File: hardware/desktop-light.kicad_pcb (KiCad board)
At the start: 2 copper layers, 100 x 100 mm, 56 parts, among them J1 Conn_01x06, J2 Conn_01x06

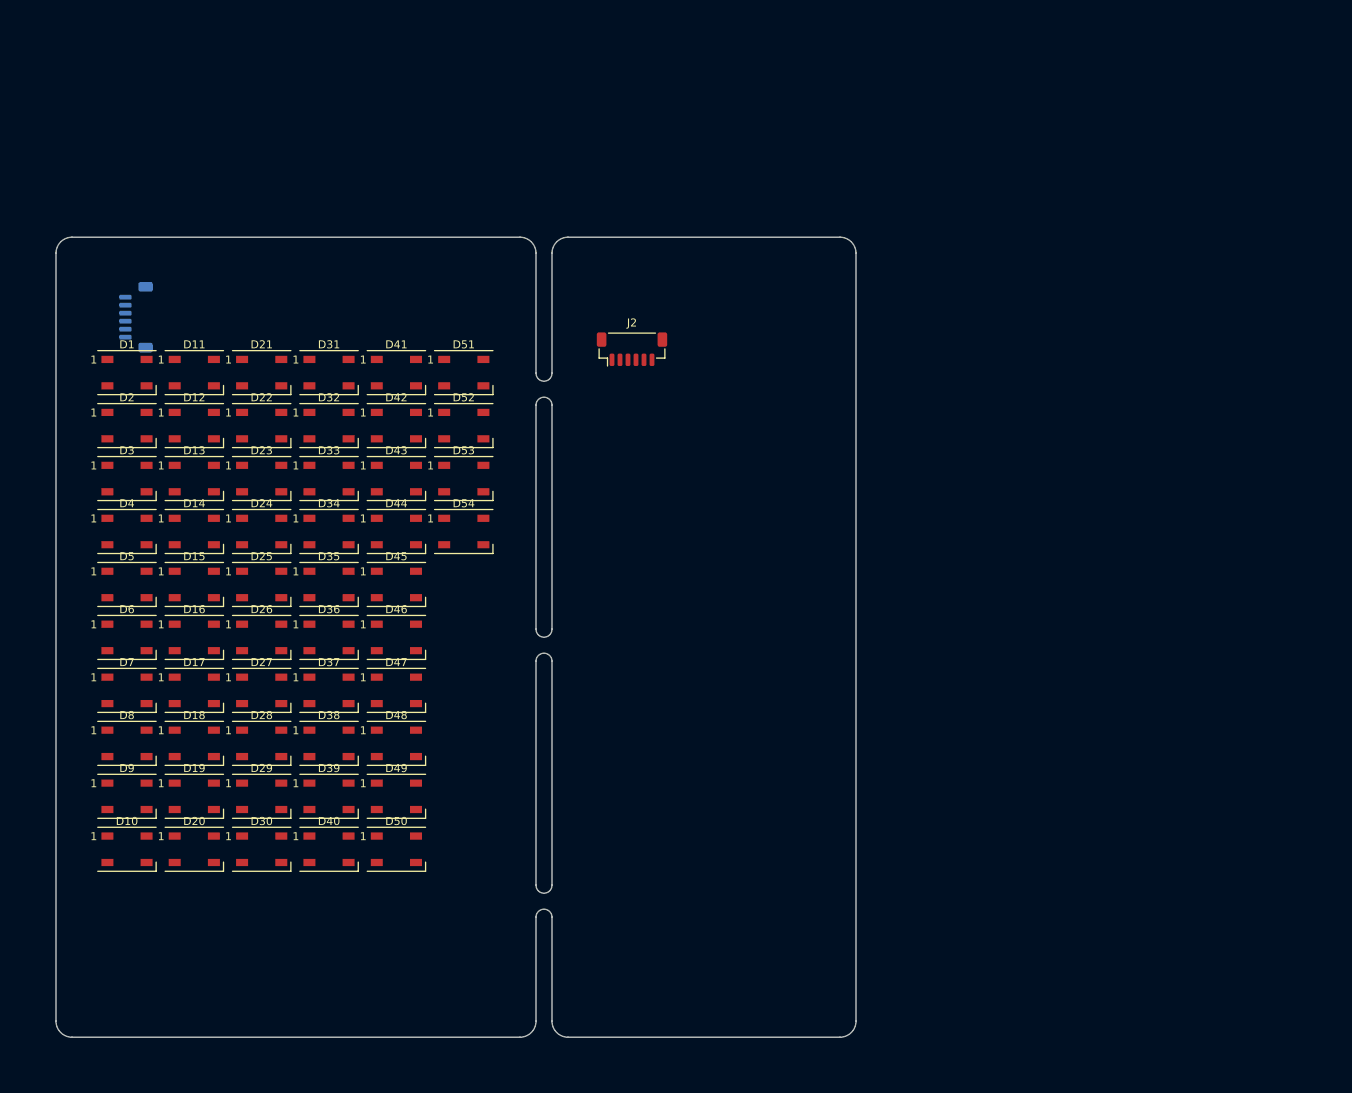
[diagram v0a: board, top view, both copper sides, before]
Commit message: add esp32
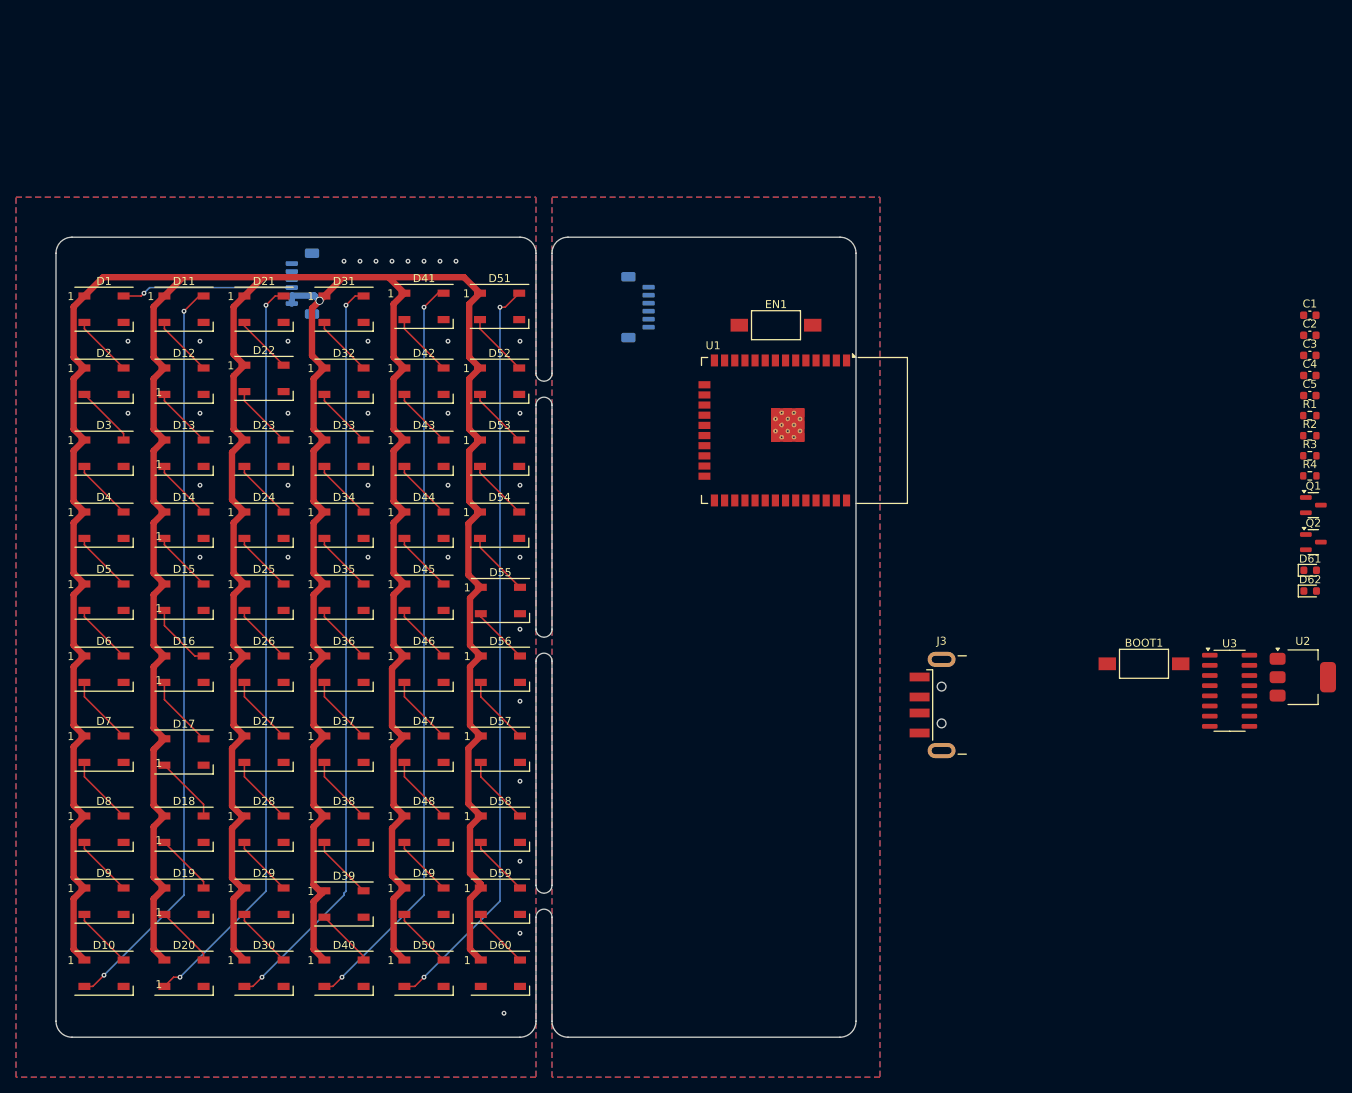
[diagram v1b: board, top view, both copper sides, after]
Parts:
- added BOOT1: SW_Push, Button_Switch_SMD:SW_SPST_FSMSM, F.Cu at (186.0, 103.3)
- added C1: C, Capacitor_SMD:C_0603_1608Metric, F.Cu at (206.7, 59.8)
- added C2: C, Capacitor_SMD:C_0603_1608Metric, F.Cu at (206.7, 62.3)
- added C3: C, Capacitor_SMD:C_0603_1608Metric, F.Cu at (206.7, 64.8)
- added C4: C, Capacitor_SMD:C_0603_1608Metric, F.Cu at (206.7, 67.3)
- added C5: C, Capacitor_SMD:C_0603_1608Metric, F.Cu at (206.7, 69.8)
- added D55: WS2812B, LED_SMD:LED_WS2812B_PLCC4_5.0x5.0mm_P3.2mm, F.Cu at (105.5, 95.4)
- added D56: WS2812B, LED_SMD:LED_WS2812B_PLCC4_5.0x5.0mm_P3.2mm, F.Cu at (105.5, 104.0)
- added D57: WS2812B, LED_SMD:LED_WS2812B_PLCC4_5.0x5.0mm_P3.2mm, F.Cu at (105.5, 114.0)
- added D58: WS2812B, LED_SMD:LED_WS2812B_PLCC4_5.0x5.0mm_P3.2mm, F.Cu at (105.5, 124.0)
- added D59: WS2812B, LED_SMD:LED_WS2812B_PLCC4_5.0x5.0mm_P3.2mm, F.Cu at (105.5, 133.0)
- added D60: WS2812B, LED_SMD:LED_WS2812B_PLCC4_5.0x5.0mm_P3.2mm, F.Cu at (105.5, 142.0)
- added D61: LED, LED_SMD:LED_0603_1608Metric, F.Cu at (206.8, 91.6)
- added D62: LED, LED_SMD:LED_0603_1608Metric, F.Cu at (206.8, 94.2)
- added EN1: SW_Push, Button_Switch_SMD:SW_SPST_FSMSM, F.Cu at (140.0, 61.0)
- added J3: USB_A, Connector_USB:USB_A_CNCTech_1001-011-01101_Horizontal, F.Cu at (167.6, 108.5)
- added Q1: BSS138, Package_TO_SOT_SMD:SOT-23, F.Cu at (207.2, 83.5)
- added Q2: BSS138, Package_TO_SOT_SMD:SOT-23, F.Cu at (207.2, 88.1)
- added R1: R_Small, Resistor_SMD:R_0603_1608Metric, F.Cu at (206.7, 72.3)
- added R2: R_Small, Resistor_SMD:R_0603_1608Metric, F.Cu at (206.7, 74.8)
- added R3: R_Small, Resistor_SMD:R_0603_1608Metric, F.Cu at (206.7, 77.3)
- added R4: R_Small, Resistor_SMD:R_0603_1608Metric, F.Cu at (206.7, 79.8)
- added U1: ESP32-WROOM-32, RF_Module:ESP32-WROOM-32, F.Cu at (140.6, 74.2)
- added U2: AMS1117-3.3, Package_TO_SOT_SMD:SOT-223-3_TabPin2, F.Cu at (205.8, 105.0)
- added U3: CH340C, Package_SO:SOIC-16_3.9x9.9mm_P1.27mm, F.Cu at (196.7, 106.7)
- J2: moved to B.Cu
- moved J1 21.2 mm to (80.8, 55.8)
- moved D50 15.9 mm to (96.0, 142.0)
- moved D10 15.8 mm to (56.0, 142.0)
- moved D40 15.6 mm to (86.0, 142.0)
- moved D20 15.5 mm to (66.0, 142.0)
- moved D30 15.5 mm to (76.0, 142.0)
- moved D39 13.6 mm to (86.0, 133.3)
- moved D49 13.6 mm to (96.0, 133.0)
- moved D9 13.4 mm to (56.0, 133.0)
- moved D19 13.2 mm to (66.0, 133.0)
- moved D29 13.1 mm to (76.0, 133.0)
- moved D48 11.3 mm to (96.0, 124.0)
- moved D8 11.1 mm to (56.0, 124.0)
- moved D38 10.9 mm to (86.0, 124.0)
- moved D18 10.8 mm to (66.0, 124.0)
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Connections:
- D54 pad 2: unconnected-(D54-DOUT-Pad2) -> Net-(D54-DOUT)
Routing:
- net +5V: track 0.00 -> 629.9 mm, vias 0 -> 1
- net Net-(D40-DOUT): track 0.00 -> 93.8 mm, vias 0 -> 2
- net Net-(D50-DOUT): track 0.00 -> 93.7 mm, vias 0 -> 2
- net Net-(D30-DOUT): track 0.00 -> 93.7 mm, vias 0 -> 2
- net Net-(D20-DOUT): track 0.00 -> 93.6 mm, vias 0 -> 2
- net Net-(D10-DOUT): track 0.00 -> 93.4 mm, vias 0 -> 2
- net Net-(D1-DIN): track 0.00 -> 21.5 mm, vias 0 -> 1
- net Net-(D16-DOUT): track 0.00 -> 9.08 mm
- net Net-(D7-DOUT): track 0.00 -> 8.73 mm
- net Net-(D6-DOUT): track 0.00 -> 8.73 mm
- net Net-(D57-DOUT): track 0.00 -> 8.73 mm
- net Net-(D56-DOUT): track 0.00 -> 8.73 mm
- net Net-(D47-DOUT): track 0.00 -> 8.73 mm
- net Net-(D46-DOUT): track 0.00 -> 8.73 mm
- net Net-(D37-DOUT): track 0.00 -> 8.73 mm
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- added copper zone on B.Cu, net GND
- added copper zone on F.Cu, net GND

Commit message: add clock
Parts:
- added BT1: Battery_Cell, Battery:BatteryHolder_LINX_BAT-HLD-012-SMT, F.Cu at (184.4, 27.4)
- added BTN1: SW_Push, Button_Switch_SMD:SW_SPST_FSMSM, F.Cu at (121.0, 125.0)
- added BTN2: SW_Push, Button_Switch_SMD:SW_SPST_FSMSM, F.Cu at (140.0, 107.0)
- added BTN3: SW_Push, Button_Switch_SMD:SW_SPST_FSMSM, F.Cu at (140.0, 141.0)
- added C6: C_Small, Capacitor_SMD:C_0603_1608Metric, F.Cu at (192.2, 36.0)
- added J4: Barrel_Jack, Connector_BarrelJack:BarrelJack_Wuerth_6941xx301002, B.Cu at (123.2, 142.0)
- added R5: R_Small, Resistor_SMD:R_0603_1608Metric, F.Cu at (192.2, 38.5)
- added R6: R_Small, Resistor_SMD:R_0603_1608Metric, F.Cu at (192.2, 41.0)
- added R7: R_Small, Resistor_SMD:R_0603_1608Metric, F.Cu at (145.0, 85.0)
- added R8: R_Small, Resistor_SMD:R_0603_1608Metric, F.Cu at (143.0, 85.0)
- added R9: R_Small, Resistor_SMD:R_0603_1608Metric, F.Cu at (141.0, 85.0)
- added U4: PCF8523T, Package_SO:SOIC-8_3.9x4.9mm_P1.27mm, F.Cu at (185.9, 38.1)
- added Y1: ABS2532768KHZ6T, Crystal:Crystal_SMD_Abracon_ABS25-4Pin_8.0x3.8mm, F.Cu at (178.1, 39.8)
- J3: value USB_A -> USB_B_Micro; footprint Connector_USB:USB_A_CNCTech_1001-011-01101_Horizontal -> Connector_USB:USB_Micro-B_Molex-105017-0001
- moved D62 92.4 mm to (114.8, 85.0)
- moved D61 91.0 mm to (121.0, 122.0)
- moved R3 89.1 mm to (118.0, 85.0), turned to 180 degrees
- moved U2 87.5 mm to (123.0, 76.8), turned to 90 degrees
- moved C2 82.9 mm to (127.0, 85.0), turned to 90 degrees
- moved Q1 80.1 mm to (128.1, 96.0), turned to 180 degrees
- moved Q2 79.3 mm to (128.0, 92.0), turned to 180 degrees
- moved C1 73.7 mm to (143.0, 96.8), turned to -90 degrees
- moved R2 70.5 mm to (137.0, 85.0), turned to 90 degrees
- moved R4 67.9 mm to (139.0, 85.0), turned to 90 degrees
- moved U3 63.8 mm to (134.0, 95.0), turned to 180 degrees
- moved BOOT1 62.5 mm to (142.0, 59.0)
- moved J3 25.4 mm to (146.8, 93.9), turned to 90 degrees
- moved EN1 7.28 mm to (142.0, 54.0)
- moved U1 2.00 mm to (140.6, 72.2)
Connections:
- J3 pad 4: GND -> unconnected-(J3-ID-Pad4)
- J3 pad 5: unconnected-(J3-Shield-Pad5) -> GND
- U1 pad 13: unconnected-(U1-IO14-Pad13) -> BTN1
- U1 pad 23: unconnected-(U1-IO15-Pad23) -> BTN2
- U1 pad 27: unconnected-(U1-IO16-Pad27) -> BTN3
- U1 pad 33: unconnected-(U1-IO21-Pad33) -> SDA
- U1 pad 36: unconnected-(U1-IO22-Pad36) -> SCL
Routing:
- net GND: vias 36 -> 51
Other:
- outline, holes or cut-outs redrawn

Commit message: finish wiring
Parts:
- added J5: Conn_01x06, Connector_JST:JST_SH_BM06B-SRSS-TB_1x06-1MP_P1.00mm_Vertical, B.Cu at (60.2, 144.5)
- BT1: moved to B.Cu
- moved BT1 101.6 mm to (122.5, 108.0), turned to 180 degrees
- moved C6 82.4 mm to (117.0, 69.8), turned to 180 degrees
- moved C5 79.2 mm to (129.0, 85.0), turned to 90 degrees
- moved R1 76.8 mm to (131.0, 85.0), turned to -90 degrees
- moved U4 74.9 mm to (116.0, 65.0), turned to -90 degrees
- moved R5 67.7 mm to (143.0, 85.0), turned to 90 degrees
- moved R6 64.5 mm to (145.0, 85.0), turned to 90 degrees
- moved Y1 63.2 mm to (117.0, 55.8), turned to 180 degrees
- moved C4 59.3 mm to (148.0, 59.0)
- moved C3 58.9 mm to (148.0, 61.0)
- moved R4 12.0 mm to (127.0, 85.0), turned to -90 degrees
- moved C2 8.00 mm to (135.0, 85.0)
- moved R2 4.00 mm to (133.0, 85.0)
- moved R7 4.00 mm to (141.0, 85.0), turned to 90 degrees
- moved R8 4.00 mm to (139.0, 85.0), turned to 90 degrees
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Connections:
- C6 pad 1: VCC -> +3V3
- D60 pad 2: unconnected-(D60-DOUT-Pad2) -> Net-(D60-DOUT)
- R5 pad 1: VCC -> +3V3
- R6 pad 1: VCC -> +3V3
- U4 pad 8: VCC -> +3V3
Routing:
- net +5V: track 629.9 -> 802.4 mm, vias 1 -> 6
- net +3V3: track 0.00 -> 118.5 mm, vias 0 -> 2
- net BTN1: track 0.00 -> 79.9 mm, vias 0 -> 3
- net Net-(BT1-+): track 0.00 -> 69.2 mm, vias 0 -> 1
- net BTN3: track 0.00 -> 64.4 mm, vias 0 -> 2
- net ESP32_EN: track 0.00 -> 62.8 mm, vias 0 -> 2
- net ESP32_IO0: track 0.00 -> 52.7 mm, vias 0 -> 2
- net SCL: track 0.00 -> 43.0 mm, vias 0 -> 2
- net SDA: track 0.00 -> 40.3 mm, vias 0 -> 2
- net Net-(D61-A): track 0.00 -> 38.4 mm
- net BTN2: track 0.00 -> 36.9 mm, vias 0 -> 3
- net Net-(U1-IO12): track 0.00 -> 28.4 mm, vias 0 -> 3
- net TX-PROG: track 0.00 -> 22.2 mm, vias 0 -> 2
- net Net-(U1-IO13): track 0.00 -> 21.6 mm
- net RX-PROG: track 0.00 -> 21.1 mm, vias 0 -> 2
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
